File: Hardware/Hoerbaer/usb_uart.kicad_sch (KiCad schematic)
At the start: 16 parts, among them J11 USB2_UART, Q5 S8050, Q6 S8050, U11 CH343P

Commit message: Nearly complete schematic with TLV61048 as 12V booster.
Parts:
- TP2, TP3: footprint (none) -> TestPoint:TestPoint_Pad_D1.5mm
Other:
- company: (none) -> Drachosaurus Designs
- title: (none) -> Hör Bär main
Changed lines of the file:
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@@
 (kicad_sch (version 20230121) (generator eeschema)
   (paper "A4")
+  (title_block
+    (title "Hör Bär main")
+    (rev "1.0")
+    (company "Drachosaurus Designs")
+  )
   (junction (at 105.41 64.77) (diameter 0) (color 0 0 0 0)
   )
@@
       (effects (font (size 1.27 1.27)) (justify left) hide)
     )
-    (property "Footprint" "" (at 180.34 78.74 0)
+    (property "Footprint" "TestPoint:TestPoint_Pad_D1.5mm" (at 180.34 78.74 0)
       (effects (font (size 1.27 1.27)) hide)
     )
@@
       (effects (font (size 1.27 1.27)) (justify left) hide)
     )
-    (property "Footprint" "" (at 175.26 78.74 0)
-      (effects (font (size 1.27 1.27)) hide)
-    )
+    (property "Footprint" "TestPoint:TestPoint_Pad_D1.5mm" (at 175.26 78.74 0)
+      (effects (font (size 1.27 1.27)) hide)
+    )

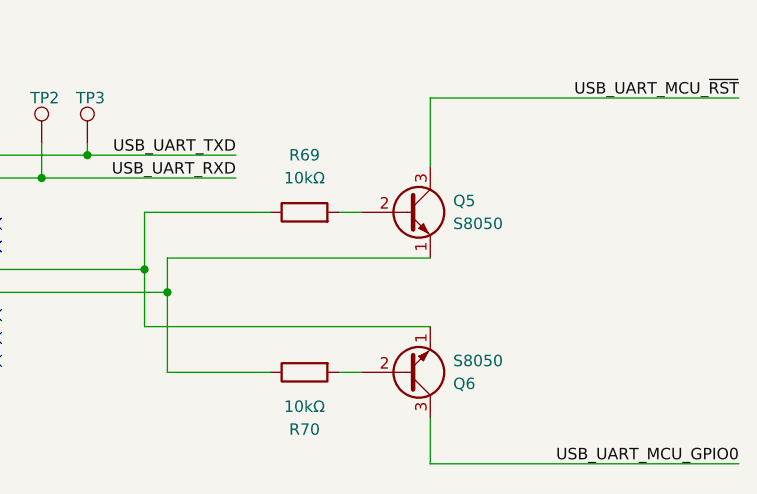
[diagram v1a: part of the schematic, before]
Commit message: Footprints, order numbers, ...
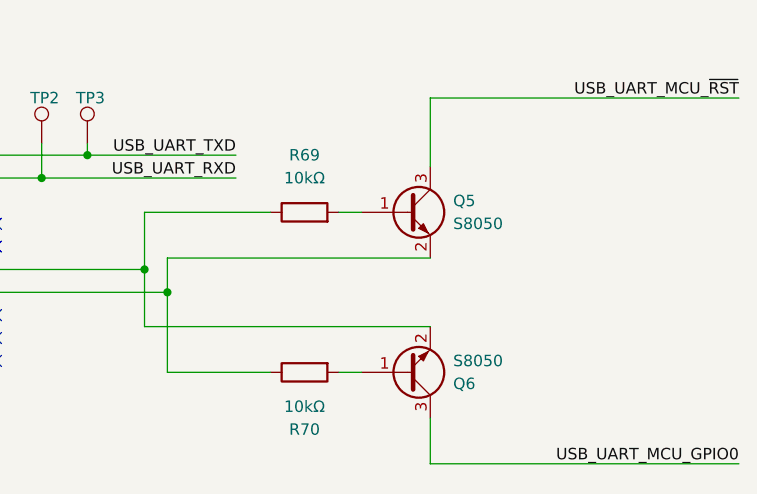
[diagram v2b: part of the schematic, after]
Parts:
- C56, C57, C58: footprint (none) -> Capacitor_SMD:C_0402_1005Metric
- Q5, Q6: footprint Package_TO_SOT_THT:TO-92_Inline -> Package_TO_SOT_SMD:SOT-23; symbol Transistor_BJT:S8050 -> Baer_Symbols:S8050_SOT23; JLCPCB (none) -> C2150; MPN (none) -> SS8050
- R51, R52, R69, R70: footprint (none) -> Resistor_SMD:R_0402_1005Metric
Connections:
- net at R70.1, U11.13 (RTS): now also Q5.2 (E); no longer Q5.1 (E)
- net at R70.2: now also Q6.1 (B); no longer Q6.2 (B)
- net at R69.2: now also Q5.1 (B); no longer Q5.2 (B)
- net at R69.1, U11.12 (DTR): now also Q6.2 (E); no longer Q6.1 (E)
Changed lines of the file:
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@@
       (effects (font (size 1.27 1.27)))
     )
-    (property "Footprint" "" (at 199.39 102.362 90)
+    (property "Footprint" "Resistor_SMD:R_0402_1005Metric" (at 199.39 102.362 90)
       (effects (font (size 1.27 1.27)) hide)
     )
@@
     )
   )
-  (symbol (lib_id "Transistor_BJT:S8050") (at 210.82 86.36 0) (unit 1)
+  (symbol (lib_id "Baer_Symbols:S8050_SOT23") (at 210.82 86.36 0) (unit 1)
     (in_bom yes) (on_board yes) (dnp no) (fields_autoplaced)
     (property "Reference" "Q5" (at 215.9 85.09 0)
@@
       (effects (font (size 1.27 1.27)) (justify left))
     )
-    (property "Footprint" "Package_TO_SOT_THT:TO-92_Inline" (at 215.9 88.265 0)
+    (property "Footprint" "Package_TO_SOT_SMD:SOT-23" (at 215.9 90.17 0)
       (effects (font (size 1.27 1.27) italic) (justify left) hide)
     )
-    (property "Datasheet" "http://www.unisonic.com.tw/datasheet/S8050.pdf" (at 210.82 86.36 0)
+    (property "Datasheet" "https://datasheet.lcsc.com/lcsc/2205060945_Guangdong-Hottech-S8050_C181158.pdf" (at 215.9 92.71 0)
       (effects (font (size 1.27 1.27)) (justify left) hide)
+    )
+    (property "JLCPCB" "C2150" (at 210.82 86.36 0)
+      (effects (font (size 1.27 1.27)) hide)
+    )
+    (property "MPN" "SS8050" (at 210.82 86.36 0)
+      (effects (font (size 1.27 1.27)) hide)
     )
     (pin "1")
@@
       (effects (font (size 1.27 1.27)) (justify left))
     )
-    (property "Footprint" "" (at 137.16 107.95 0)
+    (property "Footprint" "Capacitor_SMD:C_0402_1005Metric" (at 137.16 107.95 0)
       (effects (font (size 1.27 1.27)) hide)
     )
@@
       (effects (font (size 1.27 1.27)) (justify left))
     )
-    (property "Footprint" "" (at 86.36 72.39 0)
+    (property "Footprint" "Resistor_SMD:R_0402_1005Metric" (at 86.36 72.39 0)
       (effects (font (size 1.27 1.27)) hide)
     )
@@
     )
   )
-  (symbol (lib_id "Transistor_BJT:S8050") (at 210.82 104.14 0) (mirror x) (unit 1)
+  (symbol (lib_id "Baer_Symbols:S8050_SOT23") (at 210.82 104.14 0) (mirror x) (unit 1)
     (in_bom yes) (on_board yes) (dnp no)
     (property "Reference" "Q6" (at 215.9 105.41 0)
@@
       (effects (font (size 1.27 1.27)) (justify left))
     )
-    (property "Footprint" "Package_TO_SOT_THT:TO-92_Inline" (at 215.9 102.235 0)
+    (property "Footprint" "Package_TO_SOT_SMD:SOT-23" (at 215.9 100.33 0)
       (effects (font (size 1.27 1.27) italic) (justify left) hide)
     )
-    (property "Datasheet" "http://www.unisonic.com.tw/datasheet/S8050.pdf" (at 210.82 104.14 0)
+    (property "Datasheet" "https://datasheet.lcsc.com/lcsc/2205060945_Guangdong-Hottech-S8050_C181158.pdf" (at 215.9 97.79 0)
       (effects (font (size 1.27 1.27)) (justify left) hide)
     )
+    (property "JLCPCB" "C2150" (at 210.82 104.14 0)
+      (effects (font (size 1.27 1.27)) hide)
+    )
+    (property "MPN" "SS8050" (at 210.82 104.14 0)
+      (effects (font (size 1.27 1.27)) hide)
+    )
     (pin "1")
     (pin "2")
@@
       (effects (font (size 1.27 1.27)) (justify left))
     )
-    (property "Footprint" "" (at 86.36 69.85 0)
+    (property "Footprint" "Resistor_SMD:R_0402_1005Metric" (at 86.36 69.85 0)
       (effects (font (size 1.27 1.27)) hide)
     )
@@
       (effects (font (size 1.27 1.27)) (justify left))
     )
-    (property "Footprint" "" (at 114.3 107.95 0)
+    (property "Footprint" "Capacitor_SMD:C_0402_1005Metric" (at 114.3 107.95 0)
       (effects (font (size 1.27 1.27)) hide)
     )
@@
       (effects (font (size 1.27 1.27)) (justify left))
     )
-    (property "Footprint" "" (at 125.73 107.95 0)
+    (property "Footprint" "Capacitor_SMD:C_0402_1005Metric" (at 125.73 107.95 0)
       (effects (font (size 1.27 1.27)) hide)
     )
@@
       (effects (font (size 1.27 1.27)))
     )
-    (property "Footprint" "" (at 199.39 88.138 90)
-      (effects (font (size 1.27 1.27)) hide)
-    )
+    (property "Footprint" "Resistor_SMD:R_0402_1005Metric" (at 199.39 88.138 90)
+      (effects (font (size 1.27 1.27)) hide)
+    )

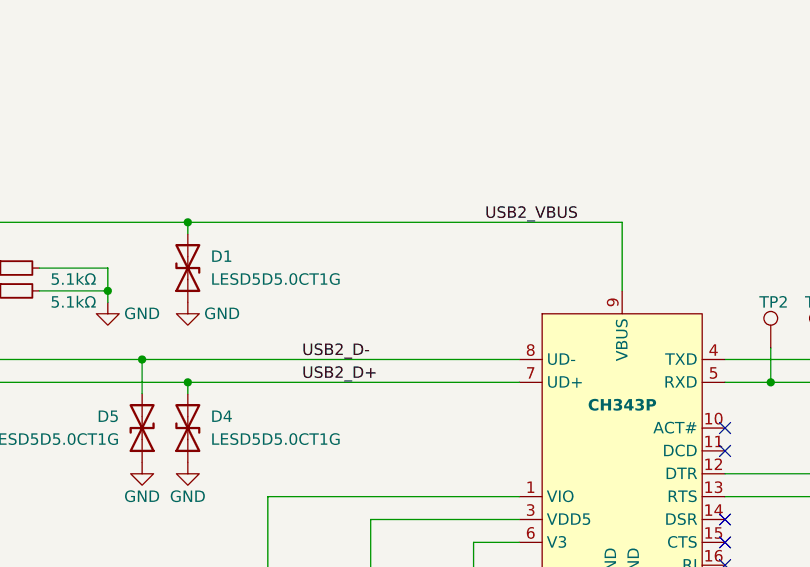
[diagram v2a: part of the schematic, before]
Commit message: More numbers, changed HBI input package, i2c addresses, layout.
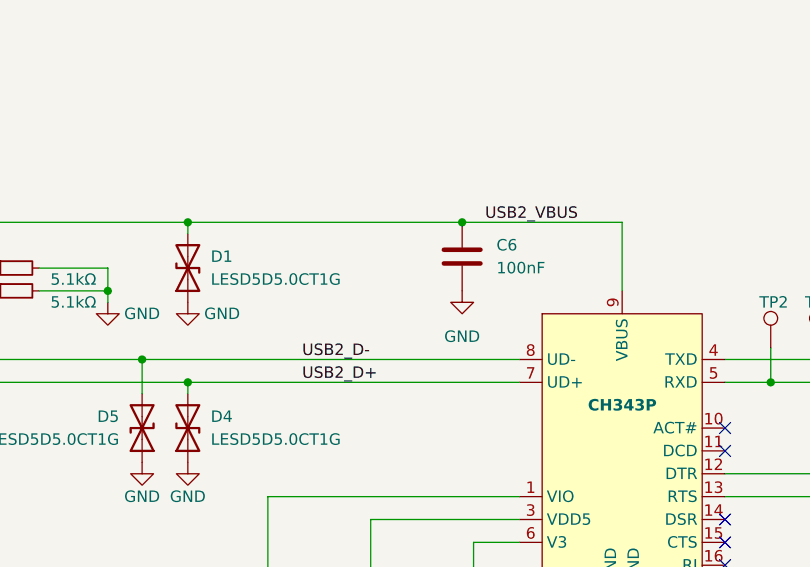
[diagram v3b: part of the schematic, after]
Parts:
- added C6: 100nF, Capacitor_SMD:C_0402_1005Metric, symbol Device:C
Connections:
- net GND: now also C6.2
- net USB2_VBUS: now also C6.1
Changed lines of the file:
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@@
   (junction (at 100.33 80.01) (diameter 0) (color 0 0 0 0)
+  )
+  (junction (at 135.89 64.77) (diameter 0) (color 0 0 0 0)
   )
   (junction (at 170.18 82.55) (diameter 0) (color 0 0 0 0)
@@
     (stroke (width 0) (type default))
   )
+  (wire (pts (xy 135.89 64.77) (xy 153.67 64.77))
+    (stroke (width 0) (type default))
+  )
   (wire (pts (xy 88.9 72.39) (xy 96.52 72.39))
     (stroke (width 0) (type default))
@@
     (stroke (width 0) (type default))
   )
-  (wire (pts (xy 105.41 64.77) (xy 153.67 64.77))
+  (wire (pts (xy 105.41 64.77) (xy 135.89 64.77))
     (stroke (width 0) (type default))
   )
@@
     )
   )
+  (symbol (lib_id "Device:C") (at 135.89 68.58 0) (unit 1)
+    (in_bom yes) (on_board yes) (dnp no) (fields_autoplaced)
+    (property "Reference" "C6" (at 139.7 67.31 0)
+      (effects (font (size 1.27 1.27)) (justify left))
+    )
+    (property "Value" "100nF" (at 139.7 69.85 0)
+      (effects (font (size 1.27 1.27)) (justify left))
+    )
+    (property "Footprint" "Capacitor_SMD:C_0402_1005Metric" (at 136.8552 72.39 0)
+      (effects (font (size 1.27 1.27)) hide)
+    )
+    (property "Datasheet" "~" (at 135.89 68.58 0)
+      (effects (font (size 1.27 1.27)) hide)
+    )
+    (pin "1")
+    (pin "2")
+    (instances
+      (project "Hoerbaer"
+        (path "/31f16f54-0469-45ae-b442-d363bf5fad3b/93ed9db9-4cd4-424a-b984-081cf903bf8d"
+          (reference "C6") (unit 1)
+        )
+        (path "/31f16f54-0469-45ae-b442-d363bf5fad3b/977d0010-d22b-463b-9672-6115e3e2a185"
+          (reference "C63") (unit 1)
+        )
+      )
+    )
+  )
   (symbol (lib_id "power:GND") (at 100.33 91.44 0) (unit 1)
     (in_bom yes) (on_board yes) (dnp no)
@@
         )
       )
+    )
+  )
+  (symbol (lib_id "power:GND") (at 135.89 72.39 0) (unit 1)
+    (in_bom yes) (on_board yes) (dnp no) (fields_autoplaced)
+    (property "Reference" "#PWR059" (at 135.89 78.74 0)
+      (effects (font (size 1.27 1.27)) hide)
+    )
+    (property "Value" "GND" (at 135.89 77.47 0)
+      (effects (font (size 1.27 1.27)))
+    )
+    (property "Footprint" "" (at 135.89 72.39 0)
+      (effects (font (size 1.27 1.27)) hide)
+    )
+    (property "Datasheet" "" (at 135.89 72.39 0)
+      (effects (font (size 1.27 1.27)) hide)
+    )
+    (pin "1")
+    (instances
+      (project "Hoerbaer"
+        (path "/31f16f54-0469-45ae-b442-d363bf5fad3b/93ed9db9-4cd4-424a-b984-081cf903bf8d"
+          (reference "#PWR059") (unit 1)
+        )
+        (path "/31f16f54-0469-45ae-b442-d363bf5fad3b/977d0010-d22b-463b-9672-6115e3e2a185"
+          (reference "#PWR0177") (unit 1)
+        )
+      )

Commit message: Layout drc error free
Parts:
- C56, C57: value 100nF -> 1uF
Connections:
- net USB2_VBUS: now also C57.1, U11.3 (VDD5)
- net VCC: now reaches C56.1, U11.1 (VIO)
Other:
- note added: "DS 5.2 p.5: Recommended dual-power supply scheme, only VIO and MCU use the same power supply, low-current consumption. VIO current is only 2uA when USB suspend/sleep."
- moved on the sheet: D4, D5

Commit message: Order numbers
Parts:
- C56, C57: JLCPCB (none) -> C726581; MPN (none) -> AC0805KKX7R6BB105
- C58, C6: JLCPCB (none) -> C458949; MPN (none) -> MT15B104K160CT
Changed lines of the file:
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@@
+      (effects (font (size 1.27 1.27)) hide)
+    )
+    (property "JLCPCB" "C458949" (at 135.89 68.58 0)
+      (effects (font (size 1.27 1.27)) hide)
+    )
+    (property "MPN" "MT15B104K160CT" (at 135.89 68.58 0)
       (effects (font (size 1.27 1.27)) hide)
     )
@@
     )
     (property "Datasheet" "~" (at 137.16 107.95 0)
+      (effects (font (size 1.27 1.27)) hide)
+    )
+    (property "JLCPCB" "C458949" (at 137.16 107.95 0)
+      (effects (font (size 1.27 1.27)) hide)
+    )
+    (property "MPN" "MT15B104K160CT" (at 137.16 107.95 0)
       (effects (font (size 1.27 1.27)) hide)
     )
@@
       (effects (font (size 1.27 1.27)) hide)
     )
+    (property "JLCPCB" "C726581" (at 114.3 107.95 0)
+      (effects (font (size 1.27 1.27)) hide)
+    )
+    (property "MPN" "AC0805KKX7R6BB105" (at 114.3 107.95 0)
+      (effects (font (size 1.27 1.27)) hide)
+    )
     (pin "1")
     (pin "2")
@@
       (effects (font (size 1.27 1.27)) hide)
     )
+    (property "JLCPCB" "C726581" (at 125.73 107.95 0)
+      (effects (font (size 1.27 1.27)) hide)
+    )
+    (property "MPN" "AC0805KKX7R6BB105" (at 125.73 107.95 0)
+      (effects (font (size 1.27 1.27)) hide)
+    )

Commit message: Renamed JLCPCB attribute to LCSC (plugin search list)
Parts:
- C56, C57: JLCPCB C726581 -> (none); LCSC (none) -> C726581
- C58, C6: JLCPCB C458949 -> (none); LCSC (none) -> C458949
- D1, D4, D5: JLCPCB C383211 -> (none); LCSC (none) -> C383211
- J11: JLCPCB C2765186 -> (none); LCSC (none) -> C2765186
- Q5, Q6: JLCPCB C2150 -> (none); LCSC (none) -> C2150
- U11: JLCPCB C2846043 -> (none); LCSC (none) -> C2846043
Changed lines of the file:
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@@
       (effects (font (size 1.27 1.27)) hide)
     )
-    (property "JLCPCB" "C383211" (at 92.71 87.63 0)
+    (property "LCSC" "C383211" (at 92.71 87.63 0)
       (effects (font (size 1.27 1.27)) hide)
     )
@@
       (effects (font (size 1.27 1.27)) hide)
     )
-    (property "JLCPCB" "C383211" (at 105.41 69.85 0)
+    (property "LCSC" "C383211" (at 105.41 69.85 0)
       (effects (font (size 1.27 1.27)) hide)
     )
@@
       (effects (font (size 1.27 1.27)) hide)
     )
-    (property "JLCPCB" "C458949" (at 135.89 68.58 0)
+    (property "LCSC" "C458949" (at 135.89 68.58 0)
       (effects (font (size 1.27 1.27)) hide)
     )
@@
       (effects (font (size 1.27 1.27)) (justify left) hide)
     )
-    (property "JLCPCB" "C2150" (at 210.82 86.36 0)
+    (property "LCSC" "C2150" (at 210.82 86.36 0)
       (effects (font (size 1.27 1.27)) hide)
     )
@@
       (effects (font (size 1.27 1.27)) hide)
     )
-    (property "JLCPCB" "C458949" (at 137.16 107.95 0)
+    (property "LCSC" "C458949" (at 137.16 107.95 0)
       (effects (font (size 1.27 1.27)) hide)
     )
@@
       (effects (font (size 1.27 1.27)) hide)
     )
-    (property "JLCPCB" "C2765186" (at 63.5 80.01 0)
+    (property "LCSC" "C2765186" (at 63.5 80.01 0)
       (effects (font (size 1.27 1.27)) hide)
     )
@@
       (effects (font (size 1.27 1.27)) (justify left) hide)
     )
-    (property "JLCPCB" "C2150" (at 210.82 104.14 0)
+    (property "LCSC" "C2150" (at 210.82 104.14 0)
       (effects (font (size 1.27 1.27)) hide)
     )
@@
       (effects (font (size 1.27 1.27)) hide)
     )
-    (property "JLCPCB" "C726581" (at 114.3 107.95 0)
+    (property "LCSC" "C726581" (at 114.3 107.95 0)
       (effects (font (size 1.27 1.27)) hide)
     )
@@
       (effects (font (size 1.27 1.27)) hide)
     )
-    (property "JLCPCB" "C726581" (at 125.73 107.95 0)
+    (property "LCSC" "C726581" (at 125.73 107.95 0)
       (effects (font (size 1.27 1.27)) hide)
     )
@@
       (effects (font (size 1.27 1.27)) hide)
     )
-    (property "JLCPCB" "C2846043" (at 153.67 125.73 0) (show_name)
+    (property "LCSC" "C2846043" (at 153.67 125.73 0) (show_name)
       (effects (font (size 1.27 1.27)) hide)
     )
@@
       (effects (font (size 1.27 1.27)) hide)
     )
-    (property "JLCPCB" "C383211" (at 97.79 87.63 0)
-      (effects (font (size 1.27 1.27)) hide)
-    )
+    (property "LCSC" "C383211" (at 97.79 87.63 0)
+      (effects (font (size 1.27 1.27)) hide)
+    )

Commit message: Resistor Order Numbers
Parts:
- R51, R52: LCSC (none) -> C25905; MPN (none) -> 0402WGF5101TCE
- R69, R70: LCSC (none) -> C25744; MPN (none) -> 0402WGF1002TCE
- TP2, TP3: now left out of the parts list
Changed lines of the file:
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@@
+      (effects (font (size 1.27 1.27)) hide)
+    )
+    (property "LCSC" "C25744" (at 199.39 104.14 0)
+      (effects (font (size 1.27 1.27)) hide)
+    )
+    (property "MPN" "0402WGF1002TCE" (at 199.39 104.14 0)
       (effects (font (size 1.27 1.27)) hide)
     )
@@
   )
   (symbol (lib_id "Connector:TestPoint") (at 175.26 78.74 0) (unit 1)
-    (in_bom yes) (on_board yes) (dnp no)
+    (in_bom no) (on_board yes) (dnp no)
     (property "Reference" "TP3" (at 173.99 73.66 0)
       (effects (font (size 1.27 1.27)) (justify left))
@@
       (effects (font (size 1.27 1.27)) hide)
     )
+    (property "LCSC" "C25905" (at 86.36 72.39 0)
+      (effects (font (size 1.27 1.27)) hide)
+    )
+    (property "MPN" "0402WGF5101TCE" (at 86.36 72.39 0)
+      (effects (font (size 1.27 1.27)) hide)
+    )
     (pin "1")
     (pin "2")
@@
   )
   (symbol (lib_id "Connector:TestPoint") (at 170.18 78.74 0) (unit 1)
-    (in_bom yes) (on_board yes) (dnp no)
+    (in_bom no) (on_board yes) (dnp no)
     (property "Reference" "TP2" (at 168.91 73.66 0)
       (effects (font (size 1.27 1.27)) (justify left))
@@
       (effects (font (size 1.27 1.27)) hide)
     )
+    (property "LCSC" "C25905" (at 86.36 69.85 0)
+      (effects (font (size 1.27 1.27)) hide)
+    )
+    (property "MPN" "0402WGF5101TCE" (at 86.36 69.85 0)
+      (effects (font (size 1.27 1.27)) hide)
+    )
     (pin "1")
     (pin "2")
@@
       (effects (font (size 1.27 1.27)) hide)
     )
+    (property "LCSC" "C25744" (at 199.39 86.36 0)
+      (effects (font (size 1.27 1.27)) hide)
+    )
+    (property "MPN" "0402WGF1002TCE" (at 199.39 86.36 0)
+      (effects (font (size 1.27 1.27)) hide)
+    )

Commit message: Fixed net tie ground plane issue.
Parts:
- J11: JLCPCB Position Offset (none) -> 0.0,1.35
- Q5, Q6: JLCPCB Rotation Offset (none) -> 180
- TP2: value TestPoint -> CH343_RXD
- TP3: value TestPoint -> CH343_TXD
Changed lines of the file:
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@@
       (effects (font (size 1.27 1.27)) (justify left))
     )
-    (property "Value" "TestPoint" (at 172.72 71.12 0)
+    (property "Value" "CH343_TXD" (at 172.72 71.12 0)
       (effects (font (size 1.27 1.27)) (justify left) hide)
     )
@@
       (effects (font (size 1.27 1.27)) hide)
     )
+    (property "JLCPCB Rotation Offset" "180" (at 210.82 86.36 0)
+      (effects (font (size 1.27 1.27)) hide)
+    )
     (pin "1")
     (pin "2")
@@
       (effects (font (size 1.27 1.27)) (justify left))
     )
-    (property "Value" "TestPoint" (at 167.64 71.12 0)
+    (property "Value" "CH343_RXD" (at 167.64 71.12 0)
       (effects (font (size 1.27 1.27)) (justify left) hide)
     )
@@
     )
     (property "MPN" "TYPE-C 16PIN 2MD(073) Copy" (at 63.5 80.01 0)
+      (effects (font (size 1.27 1.27)) hide)
+    )
+    (property "JLCPCB Position Offset" "0.0,1.35" (at 63.5 80.01 0)
       (effects (font (size 1.27 1.27)) hide)
     )
@@
       (effects (font (size 1.27 1.27)) hide)
     )
+    (property "JLCPCB Rotation Offset" "180" (at 210.82 104.14 0)
+      (effects (font (size 1.27 1.27)) hide)
+    )
